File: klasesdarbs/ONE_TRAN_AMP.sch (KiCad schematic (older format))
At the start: 10 parts, among them J1 Signal in, J2 Signal out, Q1 BC547

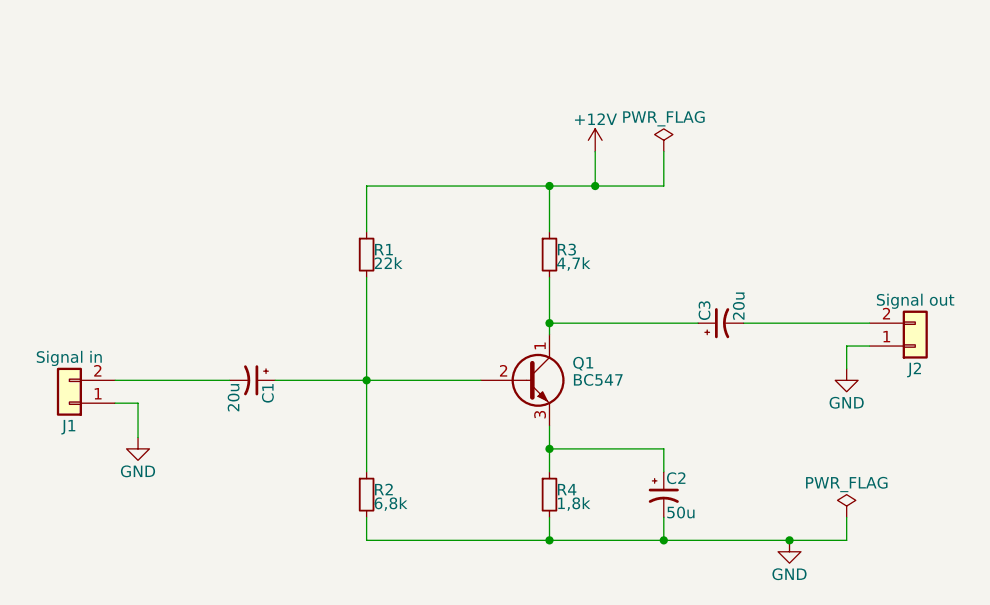
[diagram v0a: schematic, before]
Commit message: Papildinats ar pcbnew
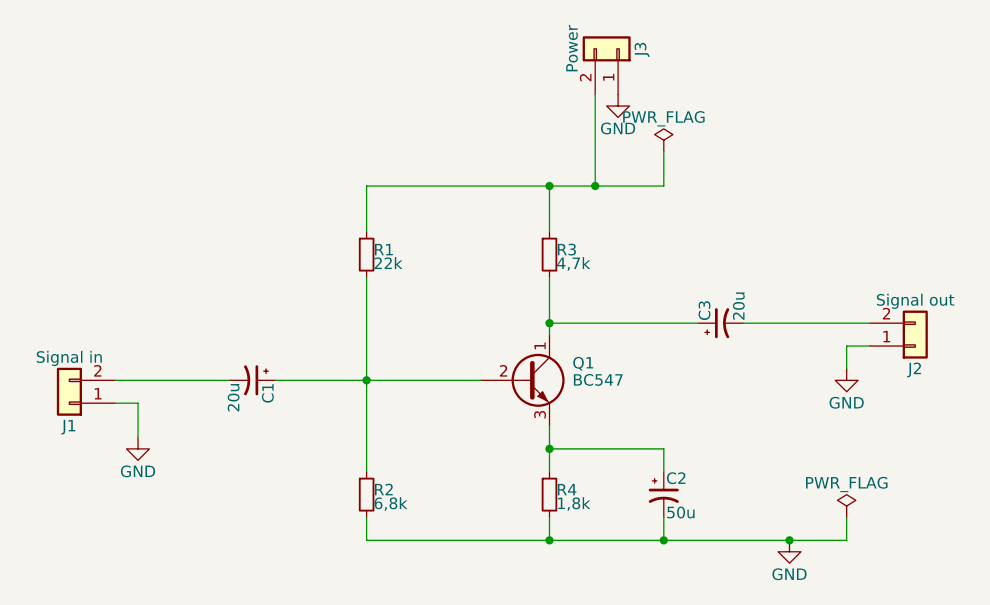
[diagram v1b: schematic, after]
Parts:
- added J3: Power, Connectors_Terminal_Blocks:TerminalBlock_Altech_AK300-2_P5.00mm, symbol Conn_01x02
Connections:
- net GND: now also J3.1 (Pin_1)
- net +12V: no longer names the net of R1.1, R3.1
- net +12V: now also J3.2 (Pin_2)
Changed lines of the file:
@@
 $EndComp
 $Comp
-L +12V #PWR01
-U 1 1 5AAA5544
-P 6250 3000
-F 0 "#PWR01" H 6250 2850 50  0001 C CNN
-F 1 "+12V" H 6250 3140 50  0000 C CNN
-F 2 "Connectors:1pin" H 6250 3000 50  0001 C CNN
-F 3 "" H 6250 3000 50  0001 C CNN
-	1    6250 3000
-	1    0    0    -1
-$EndComp
-$Comp
-L GND #PWR02
+L GND #PWR01
 U 1 1 5AAA55C8
 P 7100 4700
-F 0 "#PWR02" H 7100 4450 50  0001 C CNN
+F 0 "#PWR01" H 7100 4450 50  0001 C CNN
 F 1 "GND" H 7100 4550 50  0000 C CNN
 F 2 "Connectors:1pin" H 7100 4700 50  0001 C CNN
@@
 $EndComp
 $Comp
-L PWR_FLAG #FLG03
+L PWR_FLAG #FLG02
 U 1 1 5AAA568D
 P 6550 3000
-F 0 "#FLG03" H 6550 3075 50  0001 C CNN
+F 0 "#FLG02" H 6550 3075 50  0001 C CNN
 F 1 "PWR_FLAG" H 6550 3150 50  0000 C CNN
 F 2 "" H 6550 3000 50  0001 C CNN
@@
 $EndComp
 $Comp
-L PWR_FLAG #FLG04
+L PWR_FLAG #FLG03
 U 1 1 5AAA5721
 P 7350 4600
-F 0 "#FLG04" H 7350 4675 50  0001 C CNN
+F 0 "#FLG03" H 7350 4675 50  0001 C CNN
 F 1 "PWR_FLAG" H 7350 4750 50  0000 C CNN
 F 2 "" H 7350 4600 50  0001 C CNN
@@
 $EndComp
 $Comp
-L GND #PWR05
+L GND #PWR04
 U 1 1 5AAA581D
 P 4250 4250
-F 0 "#PWR05" H 4250 4000 50  0001 C CNN
+F 0 "#PWR04" H 4250 4000 50  0001 C CNN
 F 1 "GND" H 4250 4100 50  0000 C CNN
 F 2 "Connectors:1pin" H 4250 4250 50  0001 C CNN
@@
 $EndComp
 $Comp
-L GND #PWR06
+L GND #PWR05
 U 1 1 5AAA599C
 P 7350 3950
-F 0 "#PWR06" H 7350 3700 50  0001 C CNN
+F 0 "#PWR05" H 7350 3700 50  0001 C CNN
 F 1 "GND" H 7350 3800 50  0000 C CNN
 F 2 "Connectors:1pin" H 7350 3950 50  0001 C CNN
@@
 	5250 3150 6550 3150
 Wire Wire Line
-	6250 3150 6250 3000
+	6250 2750 6250 3150
 Wire Wire Line
 	6050 3150 6050 3350
@@
 Wire Wire Line
 	7350 3850 7450 3850
+$Comp
+L Conn_01x02 J3
+U 1 1 5AC0DB71
+P 6350 2550
+F 0 "J3" H 6350 2650 50  0000 C CNN
+F 1 "Power" H 6350 2350 50  0000 C CNN
+F 2 "Connectors_Terminal_Blocks:TerminalBlock_Altech_AK300-2_P5.00mm" H 6350 2550 50  0001 C CNN
+F 3 "http://www.fastelettronica.com/PTR_morsetti.pdf" H 6350 2550 50  0001 C CNN
+	1    6350 2550
+	0    1    -1   0
+$EndComp
+$Comp
+L GND #PWR06
+U 1 1 5AC0DD24
+P 6350 2750
+F 0 "#PWR06" H 6350 2500 50  0001 C CNN
+F 1 "GND" H 6350 2600 50  0000 C CNN
+F 2 "" H 6350 2750 50  0001 C CNN
+F 3 "" H 6350 2750 50  0001 C CNN
+	1    6350 2750
+	1    0    0    -1
+$EndComp
 $EndSCHEMATC
